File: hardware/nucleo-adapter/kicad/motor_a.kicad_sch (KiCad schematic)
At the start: 33 parts, among them J3 Motor A phase U, J4 Motor A phase V, J5 Motor A phase W, Q2 CSD16327Q3, Q3 CSD16327Q3, Q4 CSD16327Q3, Q5 CSD16327Q3, Q6 CSD16327Q3, Q7 CSD16327Q3, U4 DRV8300D (A), U5 INA180A2

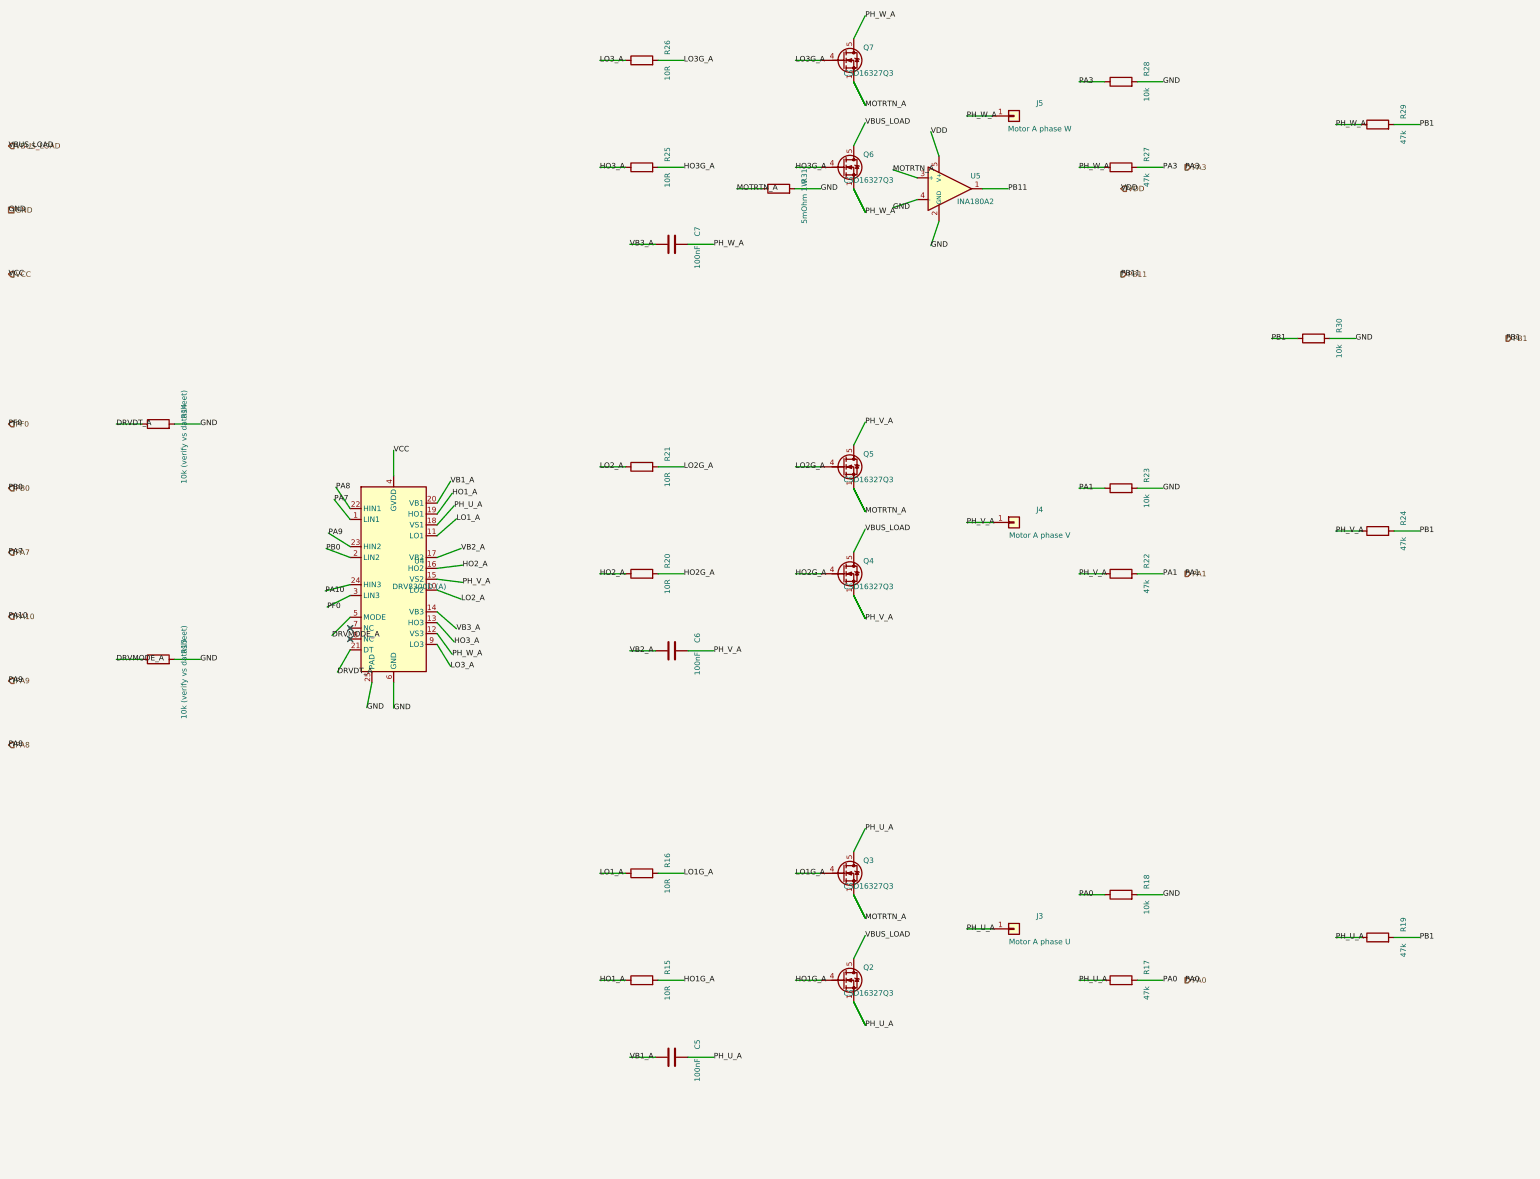
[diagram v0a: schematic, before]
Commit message: Place real Nucleo-G474RE symbol and fold it into the project libraries
Replaces the hand-authored black-box Nucleo block with the genuine
STMicroelectronics/SnapEDA symbol, wired by real CN7/CN10 pin number
rather than guessed pin names, and routed through dedicated lanes since
the real pinout doesn't line up with the sheets' pin order the way the
old placeholder did.

The symbol and its footprint were previously loose, unregistered files
(the footprint's library nickname didn't even exist in fp-lib-table).
Both now live inside the project's registered AdapterSymbols.kicad_sym
and AdapterFootprints.pretty libraries, referenced accordingly.

Co-Authored-By: Claude Sonnet 5 <noreply@anthropic.com>
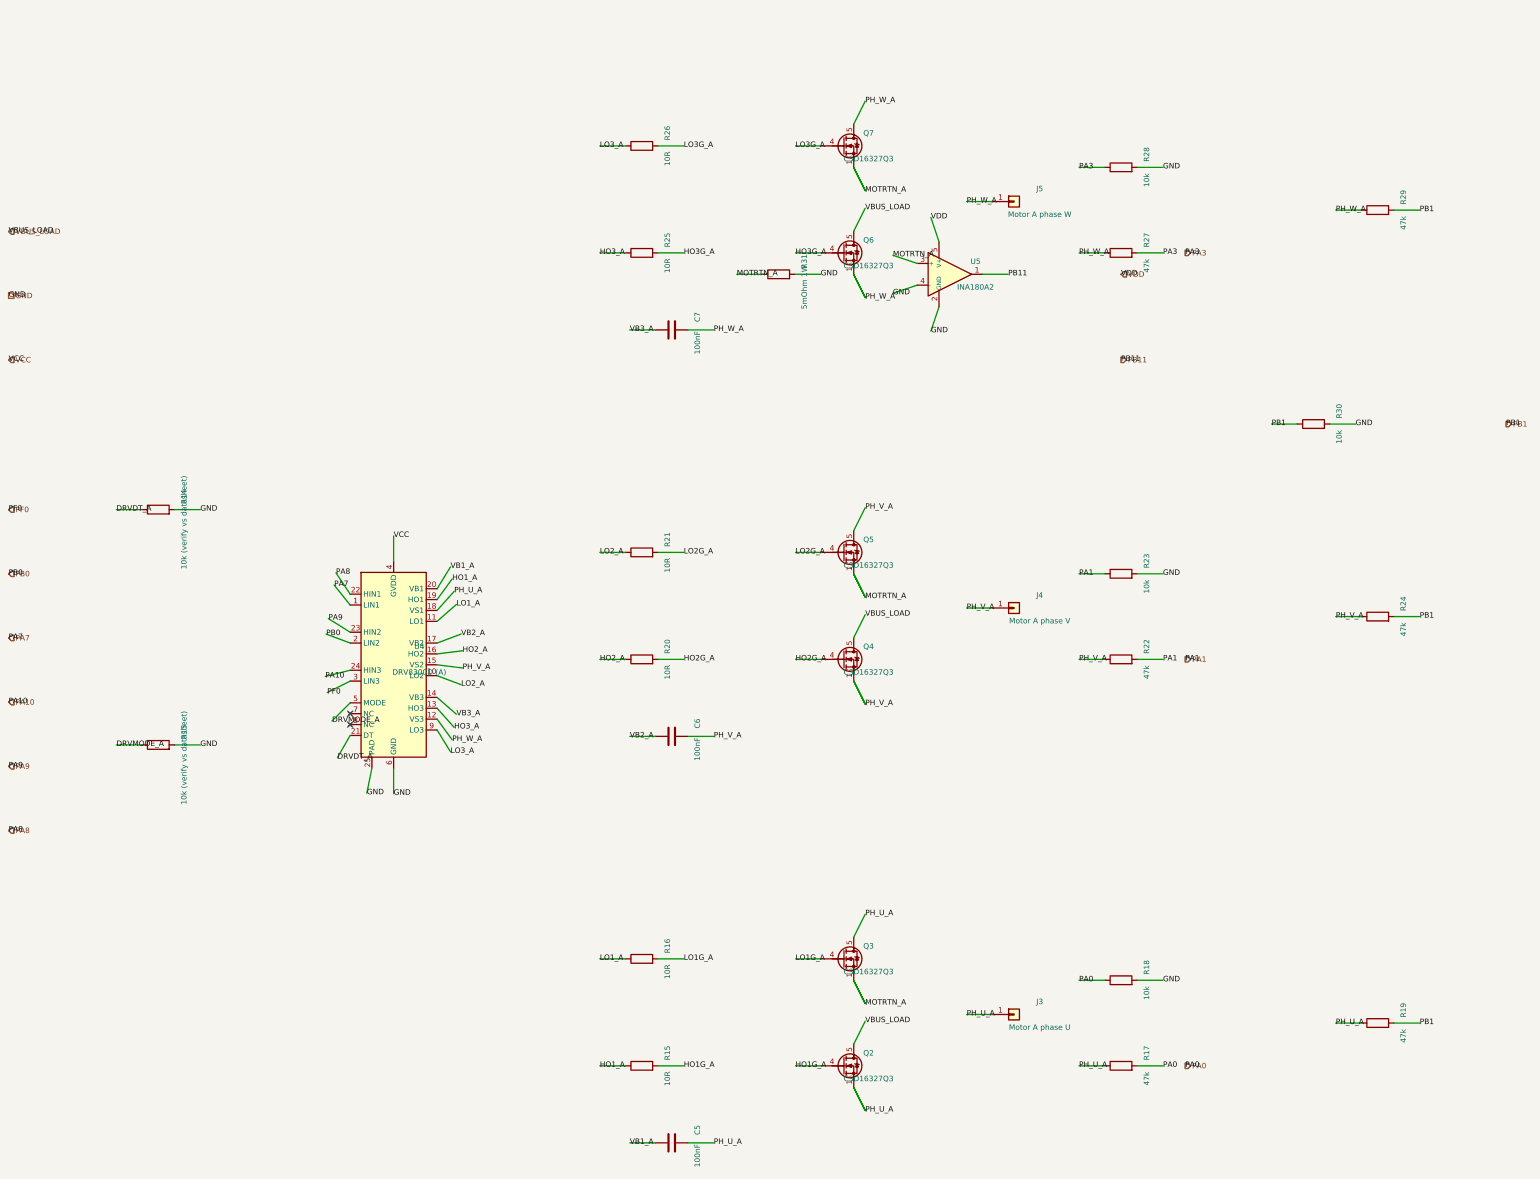
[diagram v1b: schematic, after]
